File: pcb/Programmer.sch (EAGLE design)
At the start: 47 parts, among them J1 MINI-USB-JACK, U1 TPD4S012DRYR, U10 SN74LV1T126DCKR, U2 FT232HQ, U3 SN74LV1T125DCKR, U4 SN74LV1T125DCKR, U5 SN74LV1T125DCKR, U6 SN74LV1T125DCKR, U7 SN74LV1T125DCKR, U8 SN74LV1T125DCKR, U9 SN74LV1T126DCKR, X1 SIT8021

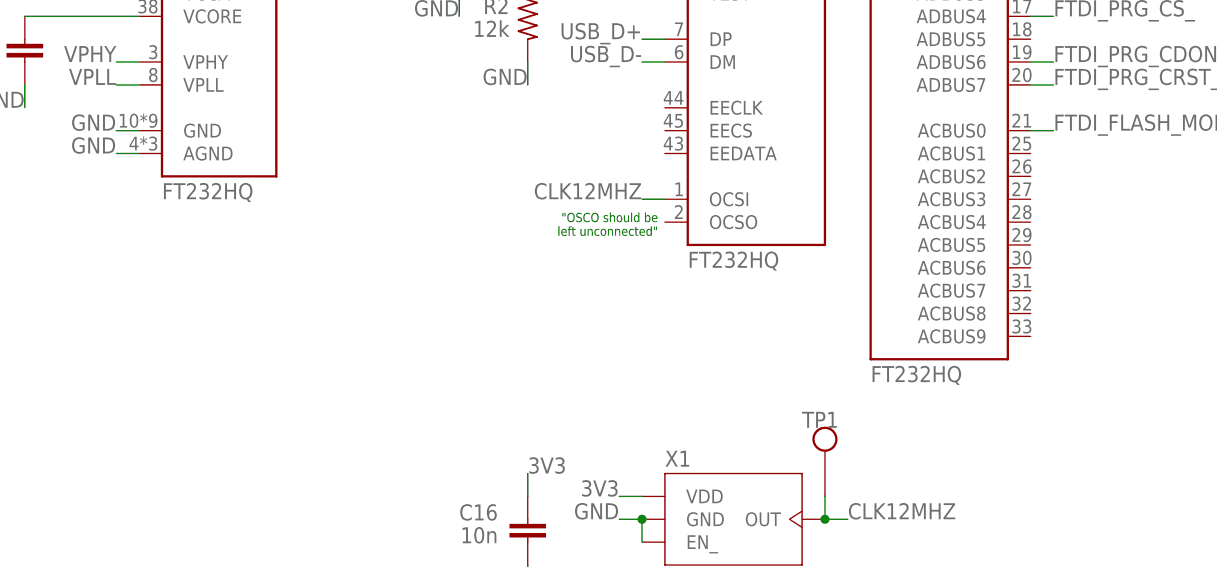
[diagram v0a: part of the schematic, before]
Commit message: Update part numbers
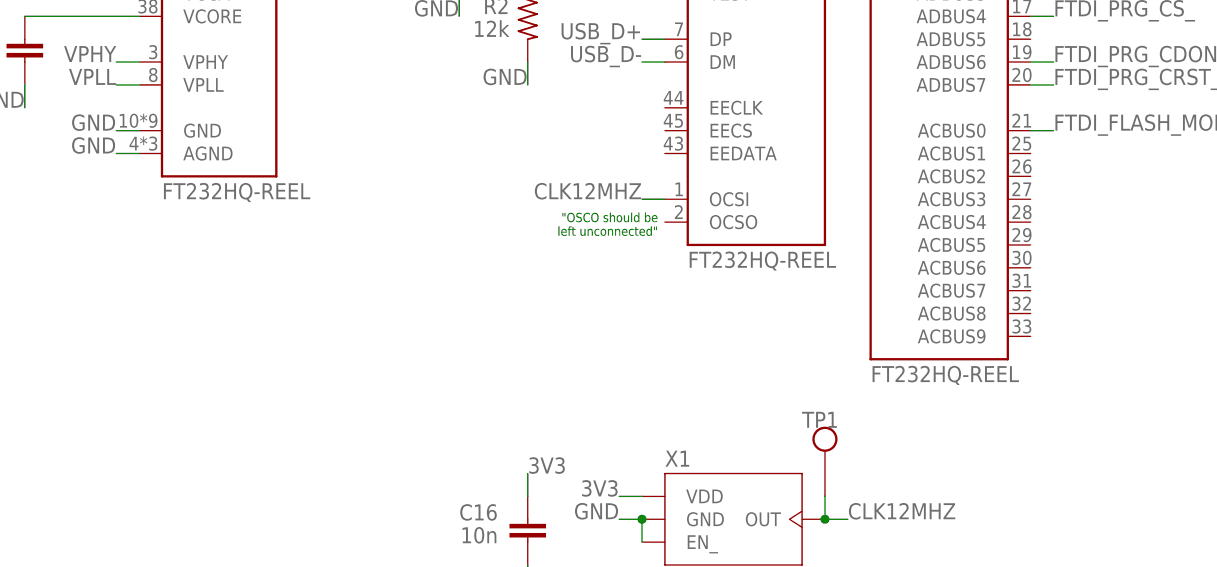
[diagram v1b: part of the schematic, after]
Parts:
- U2: PN (none) -> FT232HQ-REEL
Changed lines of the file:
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@@
 </classes>
 <parts>
-<part name="U2" library="EagleLibrary" deviceset="FT232HQ" device="" package3d_urn="urn:adsk.eagle:package:19081791/1"/>
+<part name="U2" library="EagleLibrary" deviceset="FT232HQ" device="" package3d_urn="urn:adsk.eagle:package:19081791/1">
+<attribute name="PN" value="FT232HQ-REEL"/>
+</part>
 <part name="X1" library="EagleLibrary" deviceset="SIT8021" device="">
 <attribute name="PN" value="SiT8021AI-J4-XXS-12.000000E"/>
